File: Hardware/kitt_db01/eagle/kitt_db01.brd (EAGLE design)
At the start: 74.3 x 53.3 mm, 102 parts, among them U9.00 ADNS-3080, U9.01 MIC5205-3.3YM5TR, U9.02 SI1922EDH, X9.00 RESON

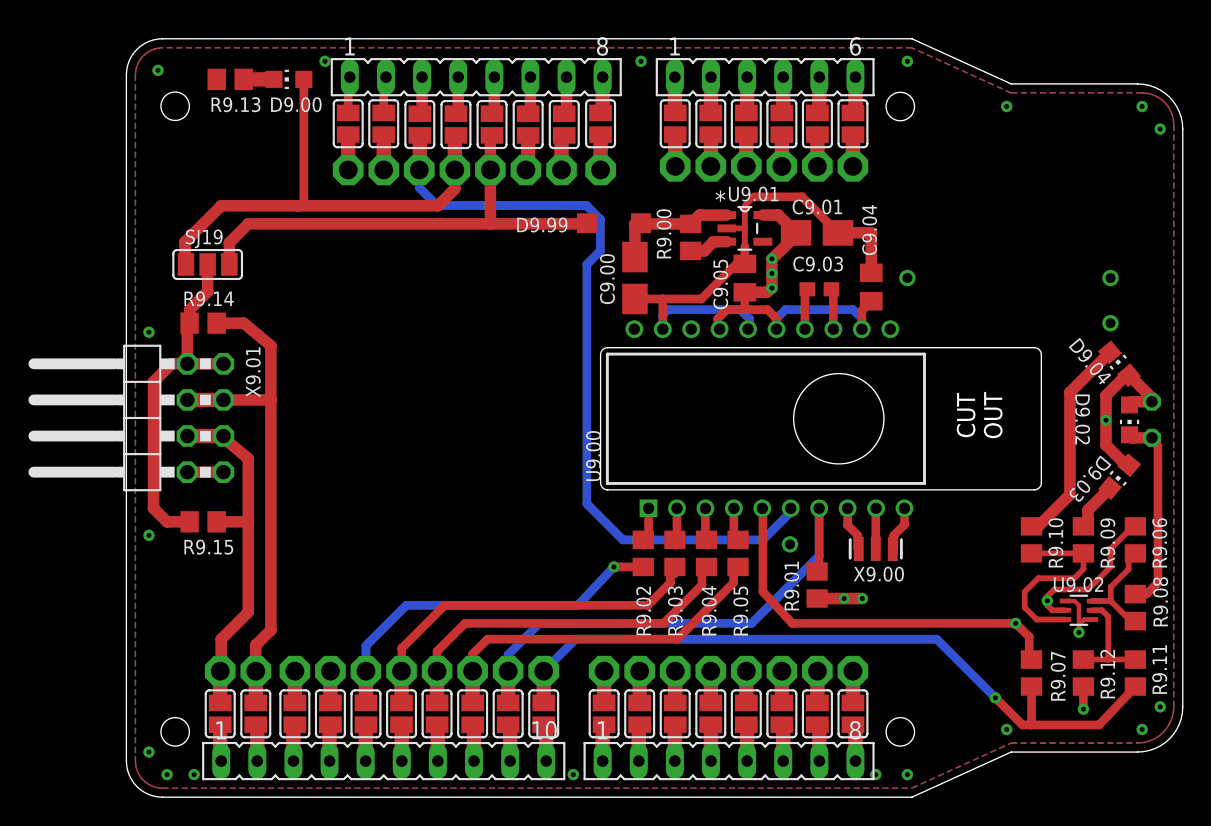
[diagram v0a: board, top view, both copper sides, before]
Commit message: snapshot of db01 board layout : so much wasted space edition -> top and botton silk screen names complete -> power plane, ground and stitching done -> some minor route optimization done
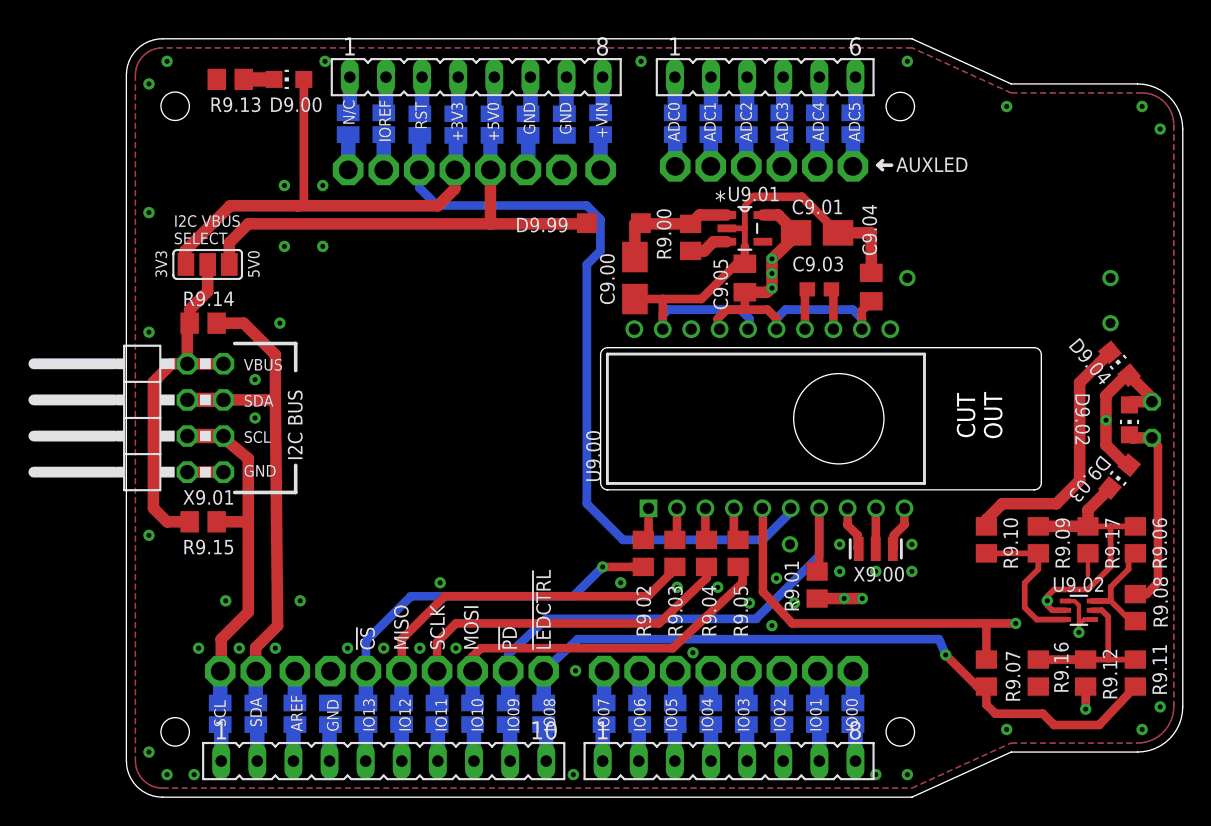
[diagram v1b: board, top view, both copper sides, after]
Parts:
- added R9.16, R9.17: 10kR, rcl:R0805
- moved R9.07 3.17 mm to (85.2, 21.7)
- moved R9.09 3.17 mm to (88.9, 31.1)
- moved R9.10 3.17 mm to (85.2, 31.1)
- moved R9.12 0.16 mm to (92.2, 21.7)
- flipped SJ1 to the bottom
- flipped SJ10 to the bottom
- flipped SJ11 to the bottom
- flipped SJ12 to the bottom
- flipped SJ13 to the bottom
- flipped SJ14 to the bottom
- flipped SJ15 to the bottom
- flipped SJ16 to the bottom
- flipped SJ17 to the bottom
- flipped SJ18 to the bottom
- flipped SJ2 to the bottom
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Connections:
- net GND: now also R9.16.2, R9.17.2
- net N$184: now also R9.16.1
- net N$4: now also R9.17.1
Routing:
- net N$185: track 14.8 -> 18.1 mm
- net N$184: track 7.97 -> 11.1 mm
- net N$187: track 3.46 -> 6.64 mm
- net N$186: track 13.9 -> 11.1 mm
- net GND: track 50.7 -> 48.1 mm, vias 23 -> 56
- net N$4: track 41.6 -> 43.5 mm
- net !LEDCTRL: track 51.2 -> 49.4 mm
- net RST: track 54.3 -> 54.9 mm
- net SDA: track 35.8 -> 36.4 mm
- net MOSI: track 25.1 -> 25.6 mm
- added copper zone on layer 3, net +3V3
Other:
- board text added: "!CS"
- board text added: "!LEDCTRL"
- board text added: "!PD"
- board text added: "3V3"
- board text added: "5V0"
- board text added: "AUXLED"
- board text added: "I2C BUS"
- board text added: "I2C VBUS SELECT"
- board text added: "IOREF"
- board text added: "MISO"
- board text added: "MOSI"
- board text added: "SCLK"
- board text added: "VBUS"
- board text removed: "IOR"

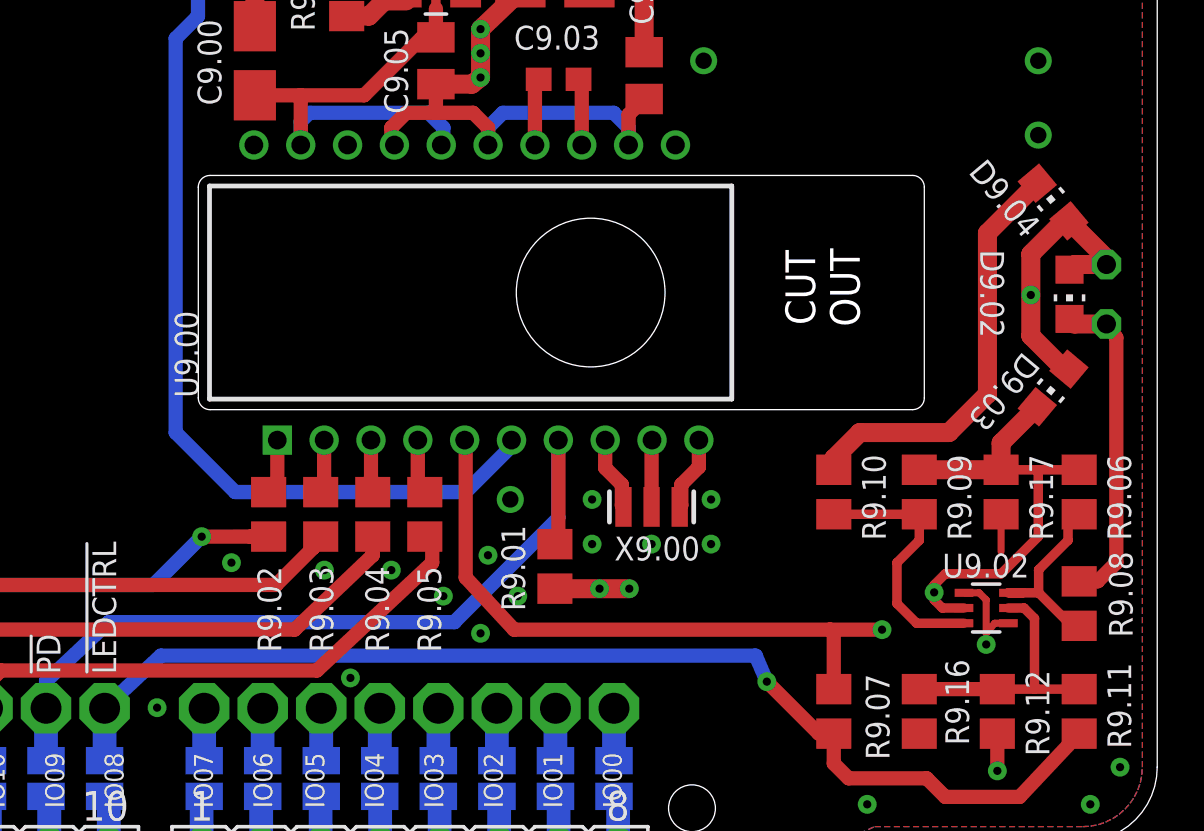
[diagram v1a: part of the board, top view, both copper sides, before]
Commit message: snapshot of db01 board layout : forgot to DRC edition -> did a DRC -> corrected various silk screen text placements
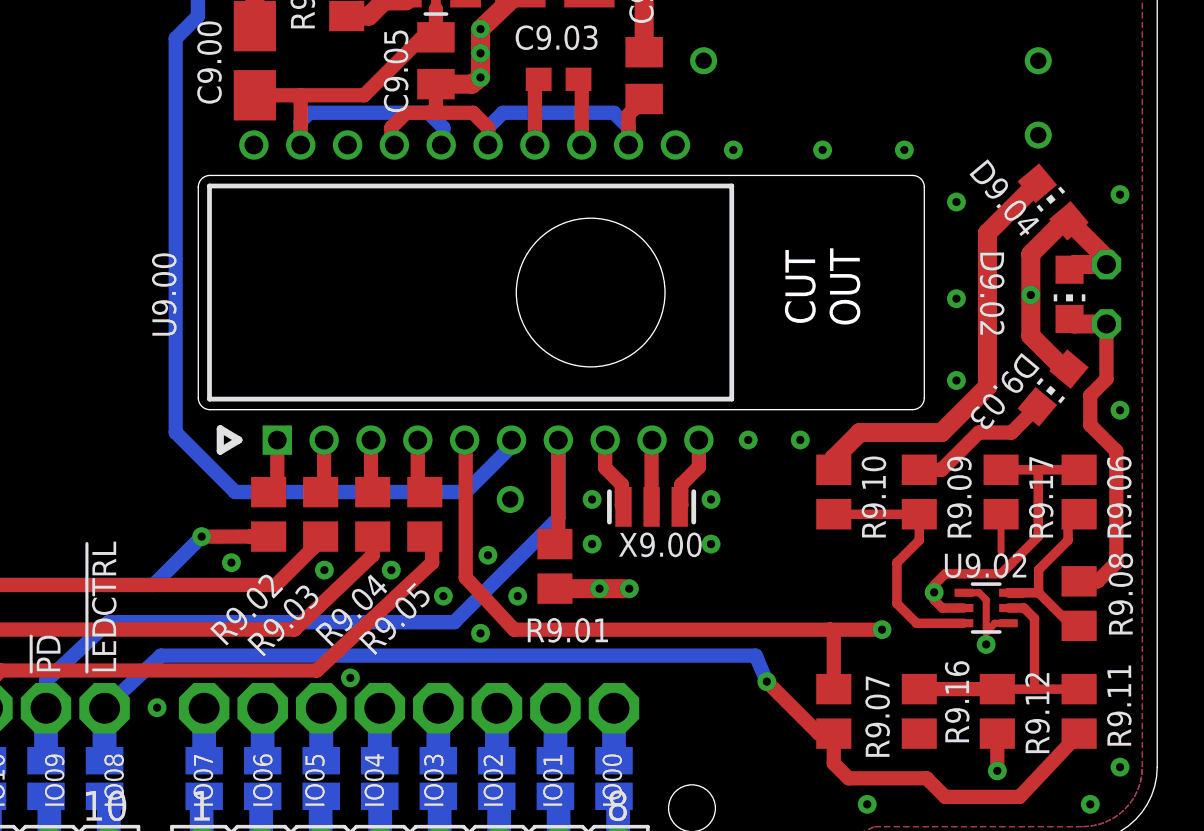
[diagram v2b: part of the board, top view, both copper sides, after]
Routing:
- net +3V3: track 160.5 -> 161.2 mm
- net N$8: track 14.0 -> 14.6 mm
- net GND: vias 56 -> 65

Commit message: added logos, text and decals on bottom side
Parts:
- added DCL1: DCL.CARRERAI, kitt.refs:DCL.LOGO-CARRERAI.W30MM
- added DCL2: DCL.OSH.COPPER'5MM', kitt.refs:DCL.LOGO-OSH.5MM
- added REF1: REF.LOGO.UASUA, kitt.refs:REF_LOGO_UASUA
- moved U$2 46.5 mm to (-70.0, -55.6)
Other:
- board text added: "2017 ESD'16"
- board text added: "KITT DB-01 R1"
- board text added: "SPFMDB"
- board text added: "c"
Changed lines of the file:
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@@
 <layers>
 <layer number="1" name="Top" color="4" fill="9" visible="yes" active="yes"/>
-<layer number="2" name="Route2" color="1" fill="3" visible="no" active="yes"/>
+<layer number="2" name="Route2" color="1" fill="3" visible="yes" active="yes"/>
 <layer number="3" name="Route3" color="24" fill="3" visible="yes" active="yes"/>
 <layer number="14" name="Route14" color="1" fill="6" visible="no" active="no"/>
@@
 <layer number="29" name="tStop" color="7" fill="3" visible="yes" active="yes"/>
 <layer number="30" name="bStop" color="7" fill="6" visible="yes" active="yes"/>
-<layer number="31" name="tCream" color="7" fill="4" visible="yes" active="yes"/>
-<layer number="32" name="bCream" color="7" fill="5" visible="yes" active="yes"/>
-<layer number="33" name="tFinish" color="6" fill="3" visible="yes" active="yes"/>
-<layer number="34" name="bFinish" color="6" fill="6" visible="yes" active="yes"/>
-<layer number="35" name="tGlue" color="7" fill="4" visible="yes" active="yes"/>
-<layer number="36" name="bGlue" color="7" fill="5" visible="yes" active="yes"/>
+<layer number="31" name="tCream" color="7" fill="4" visible="no" active="yes"/>
+<layer number="32" name="bCream" color="7" fill="5" visible="no" active="yes"/>
+<layer number="33" name="tFinish" color="6" fill="3" visible="no" active="yes"/>
+<layer number="34" name="bFinish" color="6" fill="6" visible="no" active="yes"/>
+<layer number="35" name="tGlue" color="7" fill="4" visible="no" active="yes"/>
+<layer number="36" name="bGlue" color="7" fill="5" visible="no" active="yes"/>
 <layer number="37" name="tTest" color="7" fill="1" visible="no" active="yes"/>
 <layer number="38" name="bTest" color="7" fill="1" visible="no" active="yes"/>
@@
 <layer number="47" name="Measures" color="7" fill="1" visible="yes" active="yes"/>
 <layer number="48" name="Document" color="7" fill="1" visible="yes" active="yes"/>
-<layer number="49" name="Reference" color="7" fill="1" visible="yes" active="yes"/>
+<layer number="49" name="Reference" color="7" fill="1" visible="no" active="yes"/>
 <layer number="50" name="dxf" color="16" fill="1" visible="yes" active="yes"/>
 <layer number="51" name="tDocu" color="7" fill="1" visible="no" active="yes"/>
@@
 <wire x1="59.055" y1="32.86125" x2="59.84875" y2="33.3375" width="0.3048" layer="25"/>
 <wire x1="59.84875" y1="33.3375" x2="59.055" y2="33.81375" width="0.3048" layer="25"/>
+<text x="42.06875" y="52.22875" size="1.27" layer="26" font="vector" ratio="16" rot="SMR270">KITT DB-01 R1</text>
+<text x="45.085" y="52.07" size="1.27" layer="26" font="vector" ratio="16" rot="MR270">c</text>
+<text x="44.92625" y="49.68875" size="1.27" layer="26" font="vector" ratio="16" rot="SMR270">2017 ESD'16</text>
+<circle x="44.29125" y="51.435" radius="0.9525" width="0.254" layer="26"/>
+<text x="67.46875" y="54.76875" size="1.27" layer="26" font="vector" ratio="16" rot="SMR270">SPFMDB</text>
 </plain>
 <attributes>
@@
 <attribute name="NAME" x="67.46875" y="27.37075625" size="1.016" layer="25" font="vector" rot="R225"/>
 </element>
-<element name="U$2" library="frames" package="A4L-LOC" value="" x="-40" y="-20"/>
+<element name="U$2" library="frames" package="A4L-LOC" value="" x="-70.00375" y="-55.56"/>
 <element name="X9.01" library="pinhead" package="2X04/90" value="" x="25.24125" y="39.6875" smashed="yes" rot="R90">
 <attribute name="NAME" x="32.385" y="34.6075" size="1.016" layer="25" font="vector" ratio="10" rot="R180"/>
@@
 <attribute name="NAME" x="94.615" y="29.05125" size="1.016" layer="25" font="vector" rot="R90"/>
 </element>
+<element name="DCL1" library="kitt.refs" package="DCL.LOGO-CARRERAI.W30MM" value="DCL.CARRERAI" x="53.34" y="39.52875" rot="MR270"/>
+<element name="REF1" library="kitt.refs" package="REF_LOGO_UASUA" value="REF.LOGO.UASUA" x="45.87875" y="36.195" rot="MR270"/>
+<element name="DCL2" library="kitt.refs" package="DCL.LOGO-OSH.5MM" value="DCL.OSH.COPPER'5MM'" x="63.1825" y="51.435" rot="MR270"/>
 </elements>
 <signals>
